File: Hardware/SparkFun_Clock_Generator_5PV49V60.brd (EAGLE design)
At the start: 27.9 x 25.4 mm, 74 parts, among them U1 IDT_5P49V60_CLOCK_GENERATOR, Y1 16MHz

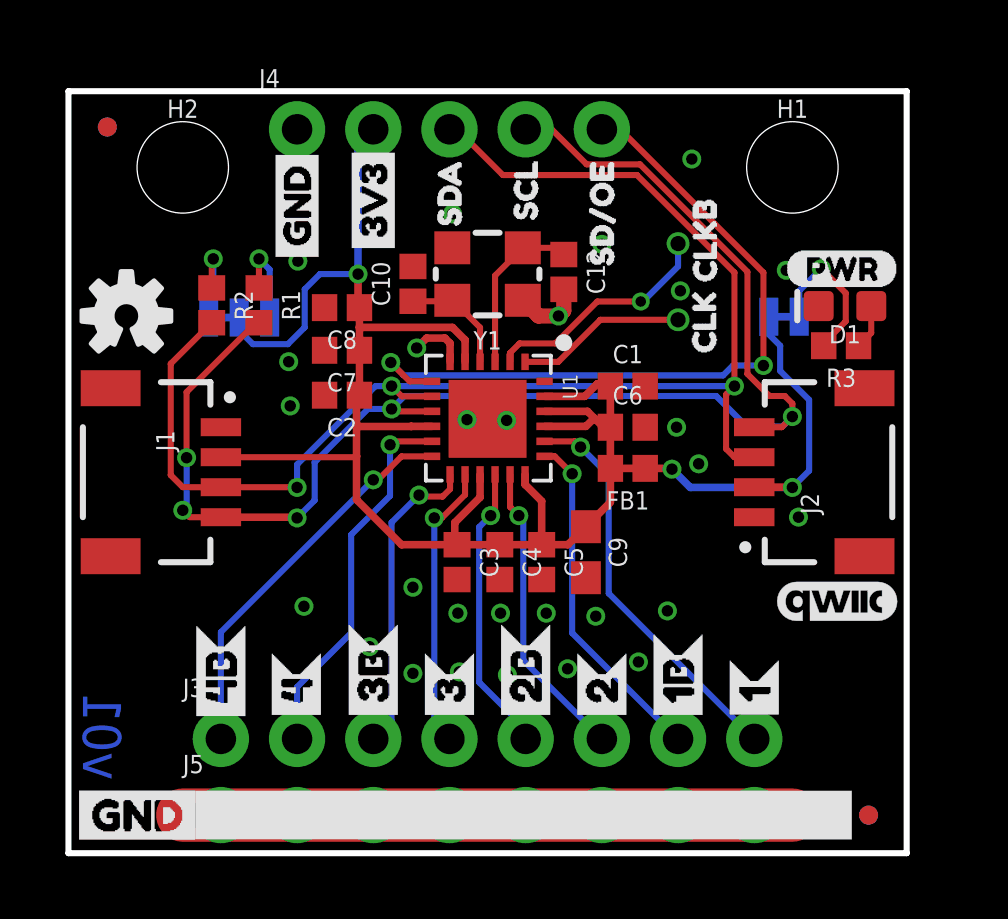
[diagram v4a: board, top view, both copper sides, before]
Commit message: Enlarges the silk on the bottom side labeling the clocks
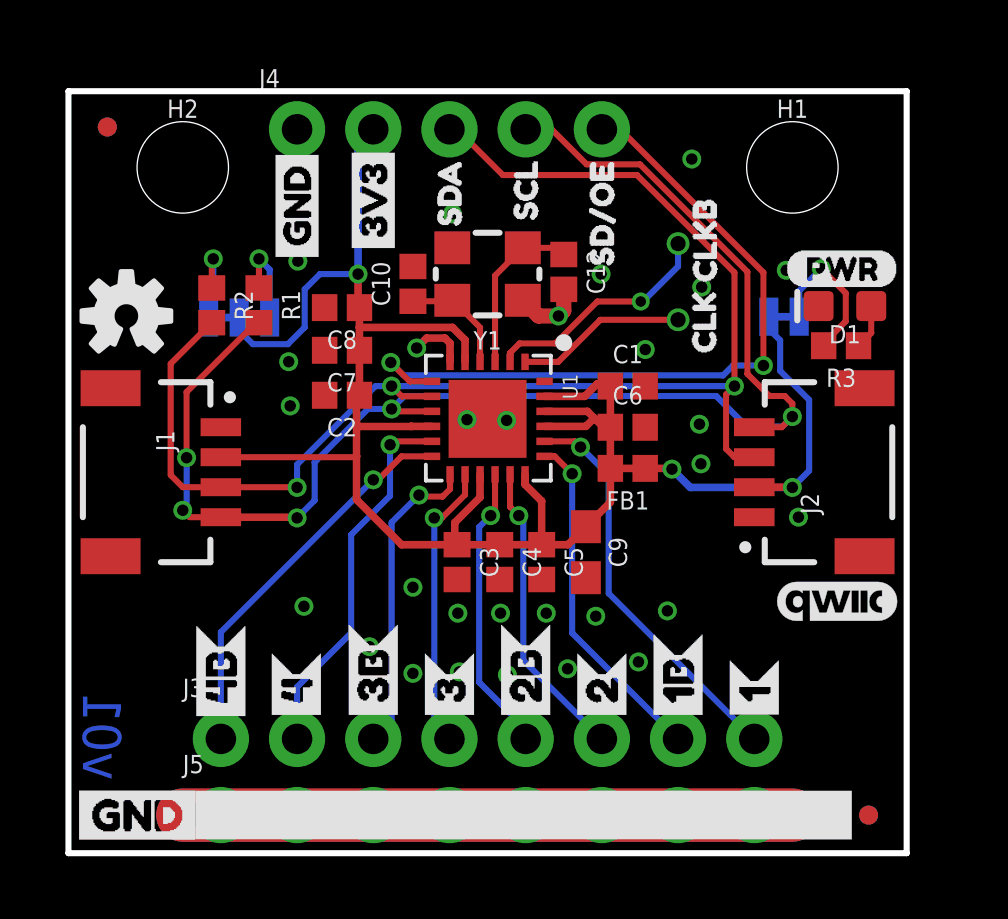
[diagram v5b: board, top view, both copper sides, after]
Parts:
- moved U$10 1.42 mm to (8.89, 10.4)
- moved U$11 1.42 mm to (3.81, 10.4)
- moved U$9 1.42 mm to (14.0, 10.4)
- moved U$8 1.35 mm to (19.1, 10.1)
- moved U$14 1.24 mm to (11.4, 9.55)
- moved U$13 1.22 mm to (16.5, 9.53)
- moved U$15 1.14 mm to (6.35, 9.42)
- moved U$12 1.12 mm to (21.6, 9.22)
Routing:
- net GND: track 24.6 -> 44.9 mm, vias 28 -> 29
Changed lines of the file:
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@@
 <layer number="45" name="Holes" color="7" fill="1" visible="yes" active="yes"/>
 <layer number="46" name="Milling" color="3" fill="1" visible="no" active="yes"/>
-<layer number="47" name="Measures" color="7" fill="1" visible="yes" active="yes"/>
+<layer number="47" name="Measures" color="7" fill="1" visible="no" active="yes"/>
 <layer number="48" name="Document" color="7" fill="1" visible="no" active="yes"/>
 <layer number="49" name="Reference" color="13" fill="1" visible="yes" active="yes"/>
@@
 <layer number="115" name="ReferenceISLANDS" color="7" fill="1" visible="no" active="no"/>
 <layer number="116" name="Patch_BOT" color="9" fill="4" visible="no" active="no"/>
-<layer number="117" name="PM_Ref" color="26" fill="1" visible="yes" active="yes"/>
+<layer number="117" name="PM_Ref" color="26" fill="1" visible="no" active="yes"/>
 <layer number="118" name="Rect_Pads" color="7" fill="1" visible="no" active="no"/>
-<layer number="119" name="PF_Ref" color="31" fill="1" visible="yes" active="yes"/>
-<layer number="120" name="WFL_Ref" color="25" fill="1" visible="yes" active="yes"/>
+<layer number="119" name="PF_Ref" color="31" fill="1" visible="no" active="yes"/>
+<layer number="120" name="WFL_Ref" color="25" fill="1" visible="no" active="yes"/>
 <layer number="121" name="_tsilk" color="7" fill="1" visible="no" active="no"/>
 <layer number="122" name="_bsilk" color="7" fill="1" visible="no" active="no"/>
@@
 <attribute name="VALUE" x="2.54" y="-0.762" size="0.6096" layer="27" font="vector" ratio="20"/>
 </element>
-<element name="U$8" library="Bottom Clock Labels" package="CLK1B1" value="" x="19.0246" y="8.7884" smashed="yes" rot="MR270"/>
-<element name="U$9" library="Bottom Clock Labels" package="CLK2B3" value="" x="13.97" y="8.9916" smashed="yes" rot="MR270"/>
-<element name="U$10" library="Bottom Clock Labels" package="CLK3B5" value="" x="8.89" y="8.9916" smashed="yes" rot="MR270"/>
-<element name="U$11" library="Bottom Clock Labels" package="CLK4B7" value="" x="3.81" y="8.9662" smashed="yes" rot="MR270"/>
-<element name="U$12" library="Bottom Clock Labels" package="CLK10" value="" x="21.59" y="8.1026" smashed="yes" rot="MR270"/>
-<element name="U$13" library="Bottom Clock Labels" package="CLK22" value="" x="16.51" y="8.3058" smashed="yes" rot="MR270"/>
-<element name="U$14" library="Bottom Clock Labels" package="CLK34" value="" x="11.43" y="8.3058" smashed="yes" rot="MR270"/>
-<element name="U$15" library="Bottom Clock Labels" package="CLK46" value="" x="6.35" y="8.2804" smashed="yes" rot="MR270"/>
+<element name="U$8" library="Bottom Clock Labels" package="CLK1B1" value="" x="19.05" y="10.1346" smashed="yes" rot="MR270"/>
+<element name="U$9" library="Bottom Clock Labels" package="CLK2B3" value="" x="13.97" y="10.414" smashed="yes" rot="MR270"/>
+<element name="U$10" library="Bottom Clock Labels" package="CLK3B5" value="" x="8.89" y="10.414" smashed="yes" rot="MR270"/>
+<element name="U$11" library="Bottom Clock Labels" package="CLK4B7" value="" x="3.81" y="10.3886" smashed="yes" rot="MR270"/>
+<element name="U$12" library="Bottom Clock Labels" package="CLK10" value="" x="21.59" y="9.2202" smashed="yes" rot="MR270"/>
+<element name="U$13" library="Bottom Clock Labels" package="CLK22" value="" x="16.4846" y="9.525" smashed="yes" rot="MR270"/>
+<element name="U$14" library="Bottom Clock Labels" package="CLK34" value="" x="11.43" y="9.5504" smashed="yes" rot="MR270"/>
+<element name="U$15" library="Bottom Clock Labels" package="CLK46" value="" x="6.35" y="9.4234" smashed="yes" rot="MR270"/>
 <element name="U$20" library="Labels" package="GND-04" value="" x="3.4544" y="1.27" smashed="yes" rot="MR0"/>
 <element name="U$21" library="Labels" package="GND-04" value="" x="-1.397" y="1.27" smashed="yes"/>
@@
 <contactref element="C7" pad="2"/>
 <via x="10.3378" y="16.8402" extent="1-16" drill="0.381"/>
-<via x="19.7358" y="12.9794" extent="1-16" drill="0.381"/>
+<via x="19.812" y="12.9794" extent="1-16" drill="0.381"/>
 <via x="23.0632" y="11.2014" extent="1-16" drill="0.381"/>
 <via x="11.5316" y="21.3106" extent="1-16" drill="0.381"/>
@@
 <via x="6.0706" y="16.383" extent="1-16" drill="0.381"/>
 <via x="6.3754" y="19.7358" extent="1-16" drill="0.381"/>
-<via x="18.9992" y="14.1986" extent="1-16" drill="0.381"/>
+<via x="19.7612" y="14.3002" extent="1-16" drill="0.381"/>
 <wire x1="11.45" y1="16.378" x2="11.45" y2="16.998" width="0.254" layer="1"/>
 <wire x1="11.45" y1="16.998" x2="11.2776" y2="17.1704" width="0.254" layer="1"/>
@@
 <via x="13.3604" y="5.9436" extent="1-16" drill="0.381"/>
 <via x="18.6944" y="8.0772" extent="1-16" drill="0.381"/>
-<via x="19.1262" y="18.7452" extent="1-16" drill="0.381"/>
-<via x="16.51" y="20.2946" extent="1-16" drill="0.381"/>
+<via x="19.8374" y="18.8722" extent="1-16" drill="0.381"/>
+<via x="16.4846" y="19.304" extent="1-16" drill="0.381"/>
 <via x="15.367" y="6.1468" extent="1-16" drill="0.381"/>
 <contactref element="J5" pad="8"/>
@@
 <wire x1="21.59" y1="1.27" x2="22.86" y2="1.27" width="1.778" layer="1"/>
 <wire x1="3.81" y1="1.27" x2="2.54" y2="1.27" width="1.778" layer="1"/>
+<wire x1="3.81" y1="1.27" x2="22.86" y2="1.27" width="1.778" layer="16"/>
+<wire x1="3.81" y1="1.27" x2="2.54" y2="1.27" width="1.778" layer="16"/>
+<via x="17.9578" y="16.7894" extent="1-16" drill="0.381"/>
 </signal>
 <signal name="3.3V">
@@
 <wire x1="22.86" y1="12.192" x2="23.4188" y2="12.7508" width="0.2032" layer="16"/>
 <wire x1="23.4188" y1="12.7508" x2="23.4188" y2="15.113" width="0.2032" layer="16"/>
-<wire x1="22.4536" y1="16.9164" x2="22.0726" y2="17.2974" width="0.2032" layer="16"/>
-<wire x1="22.0726" y1="17.2974" x2="22.0726" y2="17.8816" width="0.2032" layer="16"/>
-<wire x1="22.4536" y1="16.0782" x2="22.4536" y2="16.9164" width="0.2032" layer="16"/>
+<wire x1="22.4536" y1="17.0942" x2="22.0726" y2="17.4752" width="0.2032" layer="16"/>
+<wire x1="22.0726" y1="17.4752" x2="22.0726" y2="17.8816" width="0.2032" layer="16"/>
+<wire x1="22.4536" y1="16.0782" x2="22.4536" y2="17.0942" width="0.2032" layer="16"/>
 <wire x1="23.4188" y1="15.113" x2="22.4536" y2="16.0782" width="0.2032" layer="16"/>
 <wire x1="8.2978" y1="13.2" x2="3.81" y2="13.2" width="0.2032" layer="1"/>

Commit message: Updates crystal and 12pF parts
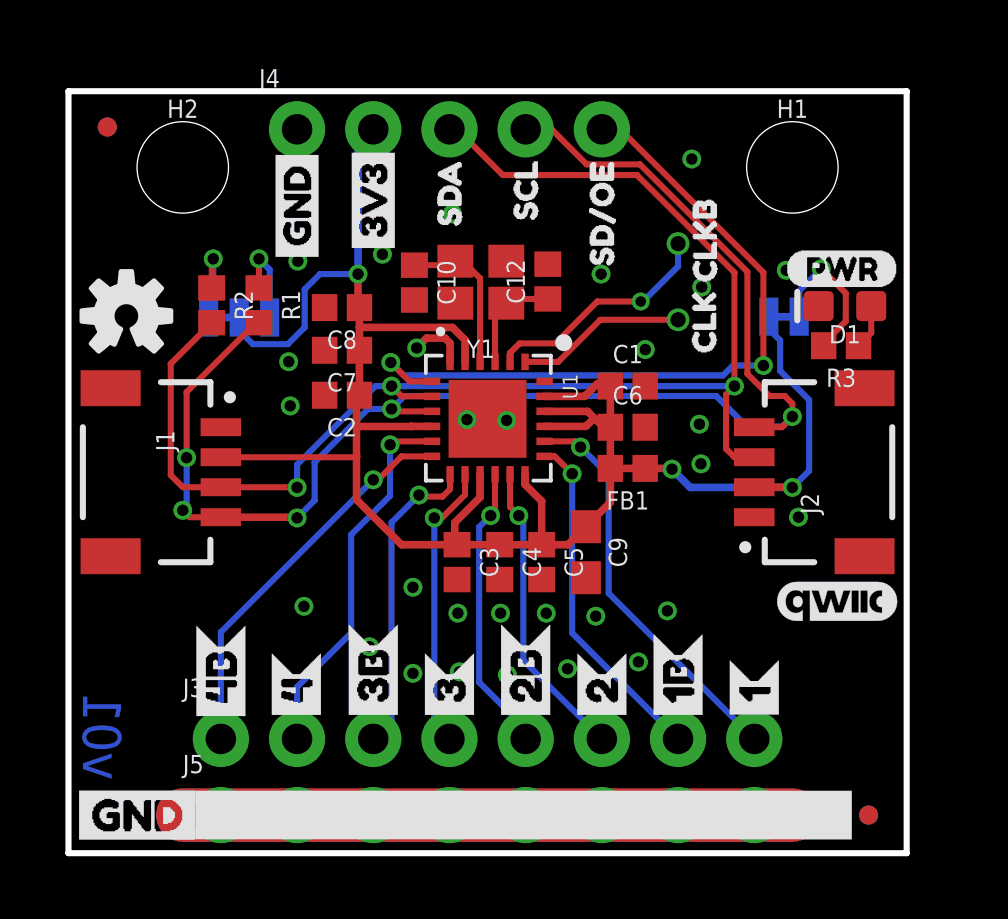
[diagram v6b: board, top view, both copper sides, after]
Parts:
- Y1: device SparkFun-Clocks:CRYSTAL-SMD-3.2X2.5MM -> SparkFun-Clocks:CRYSTAL-SMD-2X2.5MM
- moved C12 0.62 mm to (14.7, 19.1), turned to 90 degrees
- moved Y1 0.36 mm to (12.5, 19.0)
- moved C10 0.07 mm to (10.3, 19.0), turned to 270 degrees
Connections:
- net GND: now also Y1.P2, Y1.P4; no longer Y1.2, Y1.4
- net N$2: now also Y1.P1; no longer Y1.1
- net N$6: now also Y1.P3; no longer Y1.3
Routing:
- net GND: track 44.9 -> 42.6 mm
- net N$2: track 5.64 -> 3.55 mm
- net N$6: track 3.77 -> 5.27 mm
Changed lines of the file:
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@@
 <setting verticaltext="up"/>
 </settings>
-<grid distance="0.05" unitdist="inch" unit="inch" style="lines" multiple="1" display="yes" altdistance="0.001" altunitdist="inch" altunit="inch"/>
+<grid distance="0.01" unitdist="inch" unit="inch" style="lines" multiple="1" display="yes" altdistance="0.001" altunitdist="inch" altunit="inch"/>
 <layers>
 <layer number="1" name="Top" color="4" fill="1" visible="yes" active="yes"/>
@@
 <layer number="37" name="tTest" color="7" fill="1" visible="no" active="yes"/>
 <layer number="38" name="bTest" color="7" fill="1" visible="no" active="yes"/>
-<layer number="39" name="tKeepout" color="4" fill="11" visible="no" active="yes"/>
+<layer number="39" name="tKeepout" color="4" fill="11" visible="yes" active="yes"/>
 <layer number="40" name="bKeepout" color="1" fill="11" visible="no" active="yes"/>
 <layer number="41" name="tRestrict" color="4" fill="10" visible="no" active="yes"/>
@@
 <layer number="115" name="ReferenceISLANDS" color="7" fill="1" visible="no" active="no"/>
 <layer number="116" name="Patch_BOT" color="9" fill="4" visible="no" active="no"/>
-<layer number="117" name="PM_Ref" color="26" fill="1" visible="no" active="yes"/>
+<layer number="117" name="PM_Ref" color="26" fill="1" visible="yes" active="yes"/>
 <layer number="118" name="Rect_Pads" color="7" fill="1" visible="no" active="no"/>
-<layer number="119" name="PF_Ref" color="31" fill="1" visible="no" active="yes"/>
-<layer number="120" name="WFL_Ref" color="25" fill="1" visible="no" active="yes"/>
+<layer number="119" name="PF_Ref" color="31" fill="1" visible="yes" active="yes"/>
+<layer number="120" name="WFL_Ref" color="25" fill="1" visible="yes" active="yes"/>
 <layer number="121" name="_tsilk" color="7" fill="1" visible="no" active="no"/>
 <layer number="122" name="_bsilk" color="7" fill="1" visible="no" active="no"/>
@@
 <attribute name="VALUE" x="17.3736" y="13.589" size="0.6096" layer="27" font="vector" ratio="20" rot="R180" align="top-center"/>
 </element>
-<element name="Y1" library="SparkFun-Clocks" package="CRYSTAL-SMD-3.2X2.5MM" value="16MHz" x="12.7" y="19.304" smashed="yes" rot="R180">
-<attribute name="NAME" x="12.7" y="17.399" size="0.6096" layer="25" font="vector" ratio="20" rot="R180" align="bottom-center"/>
-<attribute name="PROD_ID" value="" x="12.7" y="19.304" size="1.778" layer="27" rot="R180" display="off"/>
-<attribute name="VALUE" value="16MHz" x="12.7" y="19.304" size="1.778" layer="27" rot="R180" display="off"/>
-</element>
-<element name="C12" library="SparkFun-Capacitors" package="0402" value="12pF" x="15.24" y="19.376" smashed="yes" rot="R270">
-<attribute name="NAME" x="16.002" y="19.376" size="0.6096" layer="25" font="vector" ratio="20" rot="R270" align="bottom-center"/>
-<attribute name="PROD_ID" value="" x="15.24" y="19.376" size="1.778" layer="27" font="vector" rot="R270" display="off"/>
-<attribute name="VALUE" value="12pF" x="14.478" y="19.376" size="0.6096" layer="27" font="vector" ratio="20" rot="R270" align="top-center"/>
-</element>
-<element name="C10" library="SparkFun-Capacitors" package="0402" value="12pF" x="10.2108" y="18.978" smashed="yes" rot="R90">
-<attribute name="NAME" x="9.4488" y="18.978" size="0.6096" layer="25" font="vector" ratio="20" rot="R90" align="bottom-center"/>
-<attribute name="PROD_ID" value="" x="10.2108" y="18.978" size="1.778" layer="27" font="vector" rot="R90" display="off"/>
-<attribute name="VALUE" value="12pF" x="10.9728" y="18.978" size="0.6096" layer="27" font="vector" ratio="20" rot="R90" align="top-center"/>
+<element name="Y1" library="SparkFun-Clocks" package="CRYSTAL-SMD-2X2.5MM" value="16MHz" x="12.4714" y="19.0246" smashed="yes" rot="R180">
+<attribute name="NAME" x="12.4714" y="17.1196" size="0.6096" layer="25" font="vector" ratio="20" rot="R180" align="bottom-center"/>
+<attribute name="PROD_ID" value="XTAL-14664" x="12.4714" y="19.0246" size="1.778" layer="27" rot="R180" display="off"/>
+<attribute name="VALUE" value="16MHz" x="12.4714" y="19.0246" size="1.778" layer="27" rot="R180" display="off"/>
+</element>
+<element name="C12" library="SparkFun-Capacitors" package="0402" value="12pF" x="14.7066" y="19.0542" smashed="yes" rot="R90">
+<attribute name="NAME" x="13.9446" y="19.0542" size="0.6096" layer="25" font="vector" ratio="20" rot="R90" align="bottom-center"/>
+<attribute name="PROD_ID" value="CAP-14665" x="14.7066" y="19.0542" size="1.778" layer="27" font="vector" rot="R90" display="off"/>
+<attribute name="VALUE" value="12pF" x="15.4686" y="19.0542" size="0.6096" layer="27" font="vector" ratio="20" rot="R90" align="top-center"/>
+</element>
+<element name="C10" library="SparkFun-Capacitors" package="0402" value="12pF" x="10.2616" y="19.0204" smashed="yes" rot="R270">
+<attribute name="NAME" x="11.0236" y="19.0204" size="0.6096" layer="25" font="vector" ratio="20" rot="R270" align="bottom-center"/>
+<attribute name="PROD_ID" value="CAP-14665" x="10.2616" y="19.0204" size="1.778" layer="27" font="vector" rot="R270" display="off"/>
+<attribute name="VALUE" value="12pF" x="9.4996" y="19.0204" size="0.6096" layer="27" font="vector" ratio="20" rot="R270" align="top-center"/>
 </element>
 <element name="D1" library="SparkFun-LED" package="LED-0603" value="RED" x="24.6126" y="18.2372" smashed="yes" rot="R180">
@@
 <via x="19.5072" y="23.1394" extent="1-16" drill="0.381"/>
 <via x="22.6568" y="19.431" extent="1-16" drill="0.381"/>
-<contactref element="Y1" pad="2"/>
-<contactref element="Y1" pad="4"/>
-<via x="15.0622" y="17.907" extent="1-16" drill="0.381"/>
+<contactref element="Y1" pad="P2"/>
+<contactref element="Y1" pad="P4"/>
 <contactref element="C10" pad="2"/>
 <contactref element="C12" pad="2"/>
-<wire x1="13.875" y1="18.429" x2="14.397" y2="17.907" width="0.508" layer="1"/>
-<wire x1="14.397" y1="17.907" x2="15.0622" y2="17.907" width="0.508" layer="1"/>
-<wire x1="15.0622" y1="17.907" x2="15.24" y2="18.0848" width="0.508" layer="1"/>
-<wire x1="15.24" y1="18.0848" x2="15.24" y2="18.796" width="0.508" layer="1"/>
 <contactref element="D1" pad="C"/>
 <via x="6.5786" y="8.2296" extent="1-16" drill="0.381"/>
@@
 <wire x1="3.81" y1="1.27" x2="2.54" y2="1.27" width="1.778" layer="16"/>
 <via x="17.9578" y="16.7894" extent="1-16" drill="0.381"/>
+<via x="9.1948" y="19.9644" extent="1-16" drill="0.381"/>
 </signal>
 <signal name="3.3V">
@@
 <signal name="N$6">
 <contactref element="U1" pad="P4"/>
-<wire x1="12.45" y1="16.378" x2="12.45" y2="17.522" width="0.2032" layer="1"/>
-<contactref element="Y1" pad="3"/>
+<contactref element="Y1" pad="P3"/>
 <contactref element="C10" pad="1"/>
-<wire x1="12.45" y1="17.522" x2="11.543" y2="18.429" width="0.2032" layer="1"/>
-<wire x1="11.543" y1="18.429" x2="11.525" y2="18.429" width="0.2032" layer="1"/>
-<wire x1="11.525" y1="18.429" x2="11.494" y2="18.398" width="0.2032" layer="1"/>
-<wire x1="11.494" y1="18.398" x2="10.2108" y2="18.398" width="0.2032" layer="1"/>
+<wire x1="12.45" y1="19.164" x2="11.8794" y2="19.7346" width="0.2032" layer="1"/>
+<wire x1="11.8794" y1="19.7346" x2="11.6254" y2="19.7346" width="0.2032" layer="1"/>
+<wire x1="12.45" y1="16.378" x2="12.45" y2="19.164" width="0.2032" layer="1"/>
+<wire x1="11.6254" y1="19.7346" x2="11.4912" y2="19.6004" width="0.2032" layer="1"/>
+<wire x1="11.4912" y1="19.6004" x2="10.2616" y2="19.6004" width="0.2032" layer="1"/>
 </signal>
 <signal name="N$2">
 <contactref element="U1" pad="P3"/>
-<contactref element="Y1" pad="1"/>
+<contactref element="Y1" pad="P1"/>
 <contactref element="C12" pad="1"/>
-<wire x1="12.95" y1="16.378" x2="12.95" y2="19.254" width="0.2032" layer="1"/>
-<wire x1="12.95" y1="19.254" x2="13.875" y2="20.179" width="0.2032" layer="1"/>
-<wire x1="13.875" y1="20.179" x2="15.017" y2="20.179" width="0.2032" layer="1"/>
-<wire x1="15.017" y1="20.179" x2="15.24" y2="19.956" width="0.2032" layer="1"/>
+<wire x1="12.95" y1="16.378" x2="12.95" y2="17.9592" width="0.2032" layer="1"/>
+<wire x1="12.95" y1="17.9592" x2="13.3254" y2="18.3346" width="0.2032" layer="1"/>
+<wire x1="13.3254" y1="18.3346" x2="13.465" y2="18.4742" width="0.2032" layer="1"/>
+<wire x1="13.465" y1="18.4742" x2="14.7066" y2="18.4742" width="0.2032" layer="1"/>
 </signal>
 <signal name="N$4">
